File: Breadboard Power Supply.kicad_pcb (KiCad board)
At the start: 2 copper layers, 53.6 x 23.2 mm, 27 parts, among them J1 USB-C, J10 Conn_01x02_Male, J11 Conn_01x02_Male, J2 Conn_02x03_Odd_Even, J3 Conn_02x03_Odd_Even, J8 Conn_01x02_Male, J9 Conn_01x02_Male, U1 LM1117-1.8, U2 LM1117-3.3

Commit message: Updated the version number.
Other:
- board text added: "7"
- board text removed: "6"
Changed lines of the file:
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@@
     (title "Breadboard Power Supply")
     (date "2023-04-30")
-    (rev "v6")
+    (rev "v7")
   )
   (layers
@@
   (gr_line (start 155.067 98.425) (end 155.067 75.184)
     (stroke (width 0.1) (type solid)) (layer "Edge.Cuts"))
-  (gr_text "6" (at 133.477 75.946) (layer "F.Cu")
+  (gr_text "7" (at 133.477 75.946) (layer "F.Cu")
     (effects (font (size 0.5 0.5) (thickness 0.08)))
   )

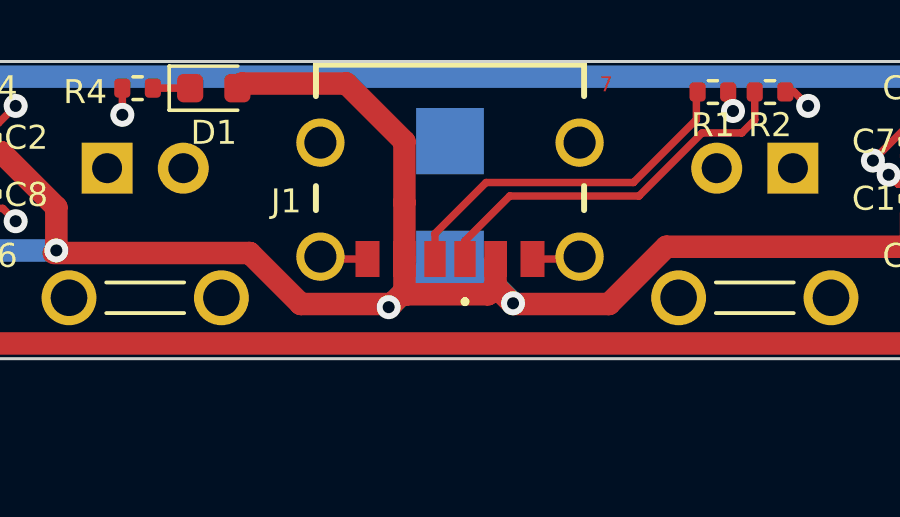
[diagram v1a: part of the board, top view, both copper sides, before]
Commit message: Replaced the Zener diode's footprint with one in the default library.
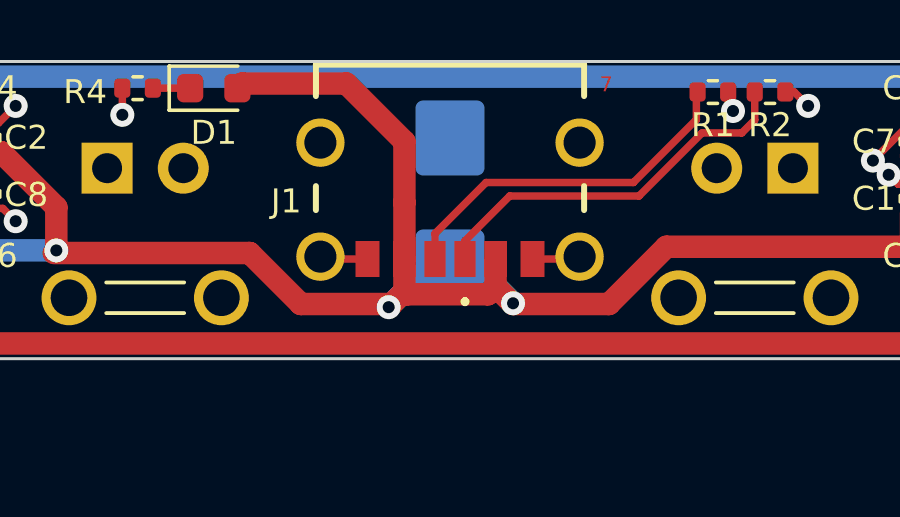
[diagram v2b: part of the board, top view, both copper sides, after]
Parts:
- D2: footprint My-Global-Footprints:SMB_STM -> Diode_SMD:D_SMB

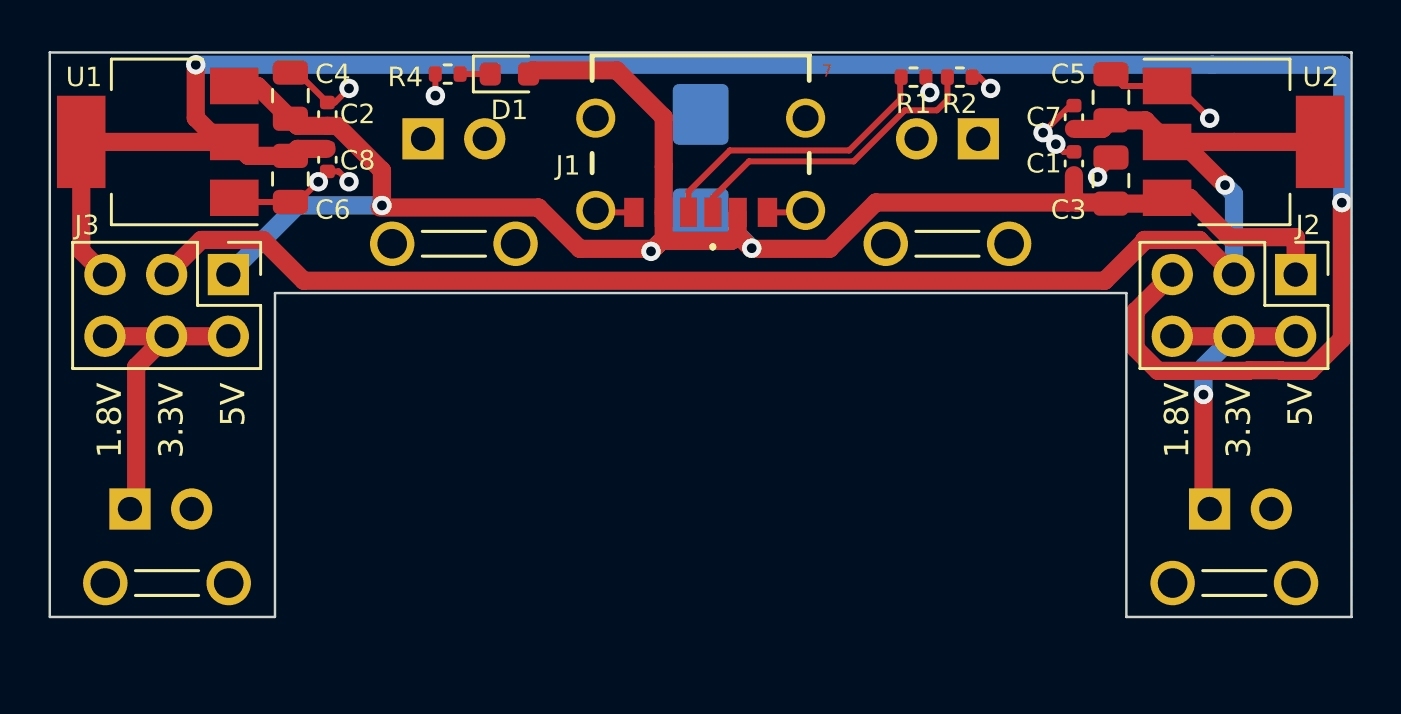
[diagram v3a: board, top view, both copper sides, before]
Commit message: Placed LEDs near voltage regulators.
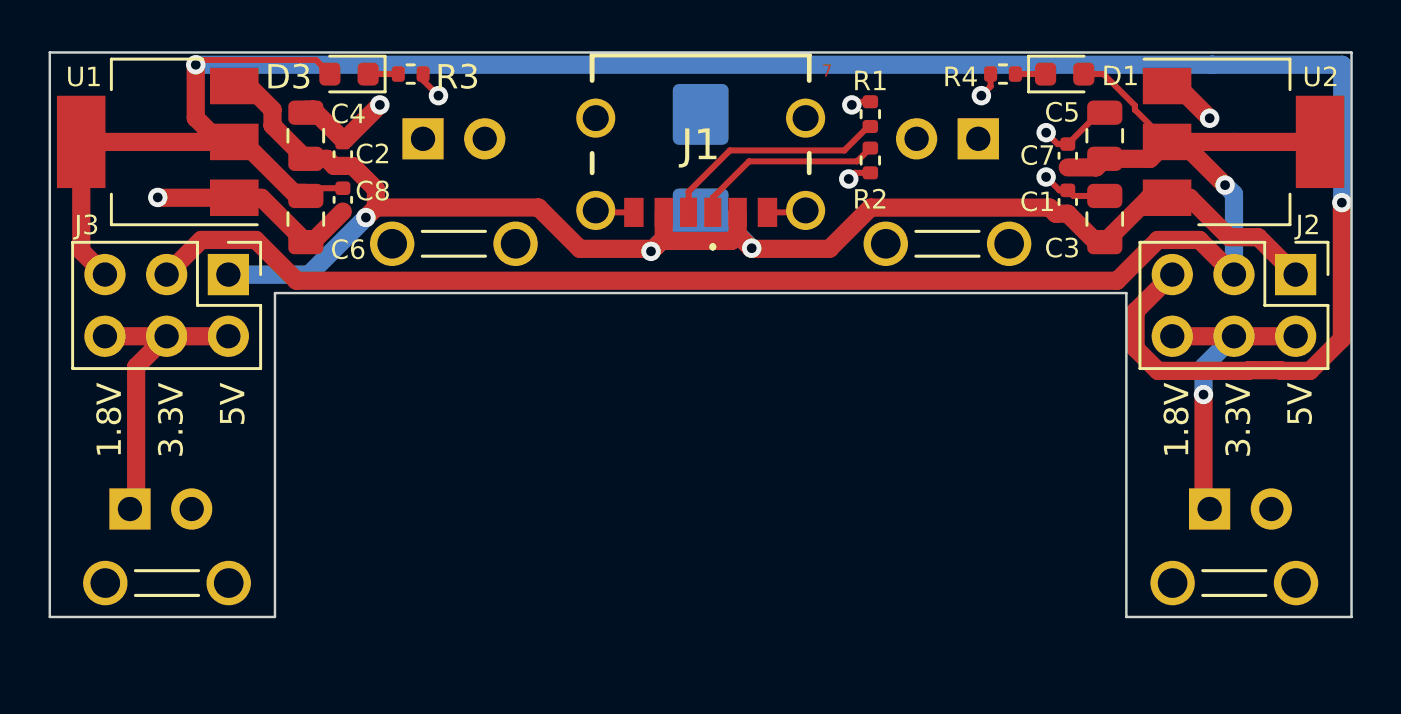
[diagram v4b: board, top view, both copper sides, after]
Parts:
- added D3: LED, LED_SMD:LED_0603_1608Metric, F.Cu at (113.8, 76.1)
- added R3: 1k, Resistor_SMD:R_0402_1005Metric, F.Cu at (116.3, 76.1)
- moved R4 22.9 mm to (140.7, 76.1)
- moved D1 22.9 mm to (143.3, 76.1)
- moved R2 5.03 mm to (135.3, 79.6), turned to -90 degrees
- moved R1 2.34 mm to (135.3, 77.7), turned to 90 degrees
- moved C2 1.77 mm to (113.5, 79.4)
- moved C4 1.77 mm to (112.0, 78.6)
- moved C6 1.77 mm to (112.0, 82.0)
- moved C8 1.77 mm to (113.5, 81.3)
- moved C3 1.61 mm to (144.9, 82.0)
- moved C7 1.61 mm to (143.4, 79.4)
- moved C1 1.61 mm to (143.4, 81.3)
- moved C5 1.61 mm to (144.9, 78.6)
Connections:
- D1 pad 2: +5V -> +3.3V
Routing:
- net +5V: track 77.5 -> 65.9 mm
- net +1V8: track 92.1 -> 99.6 mm
- net GND: track 22.3 -> 28.4 mm, vias 10 -> 9
- net Net-(J1-CC1): track 12.9 -> 7.94 mm
- net +3.3V: track 64.2 -> 69.0 mm
- net Net-(J1-CC2): track 12.1 -> 9.45 mm
- net Net-(D3-K): track 0.00 -> 1.24 mm

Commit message: Added a symbol for the OSHW logo.
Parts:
- removed REF**: OSHW-Logo_5.7x6mm_SilkScreen, Symbol:OSHW-Logo_5.7x6mm_SilkScreen
- added SYM1: Logo_Open_Hardware_Small, Symbol:OSHW-Logo_5.7x6mm_SilkScreen, B.Cu at (108.7, 78.5)

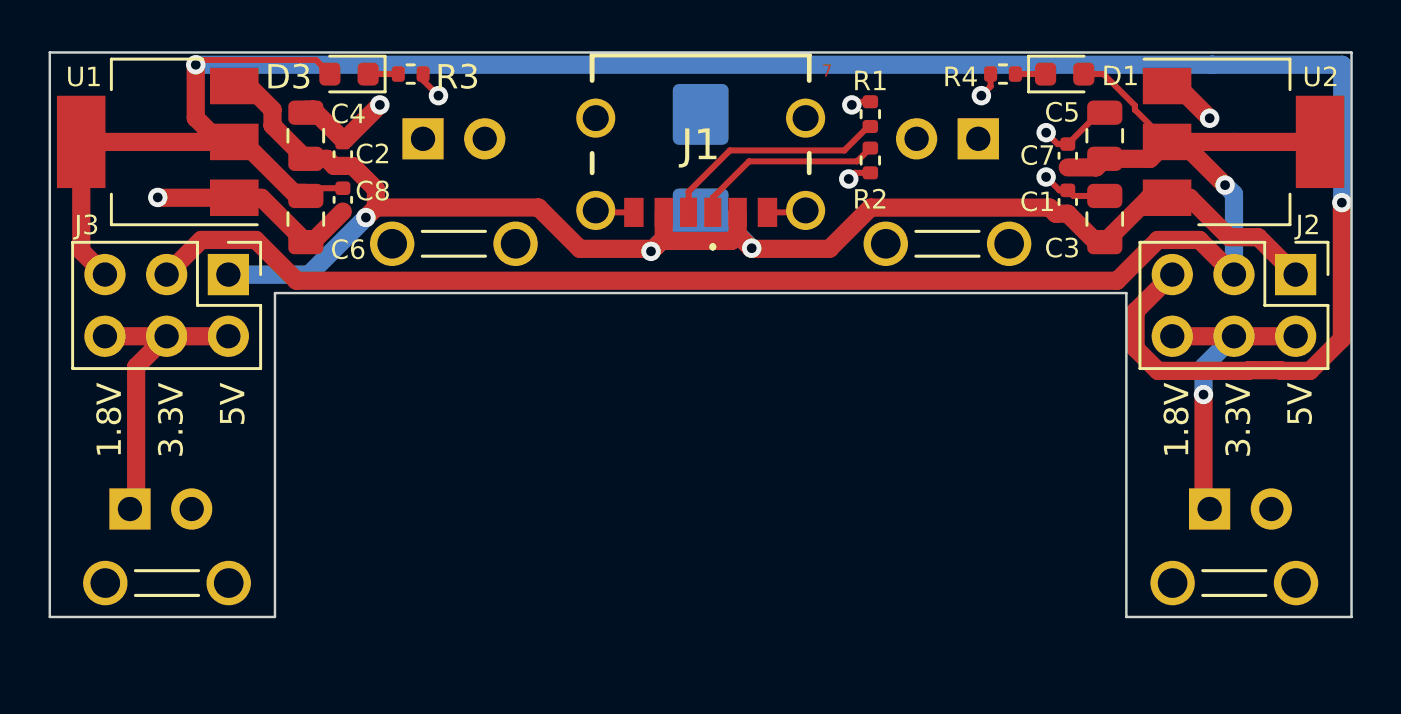
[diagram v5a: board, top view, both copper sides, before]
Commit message: Moved the USB-C to the local footprints library.
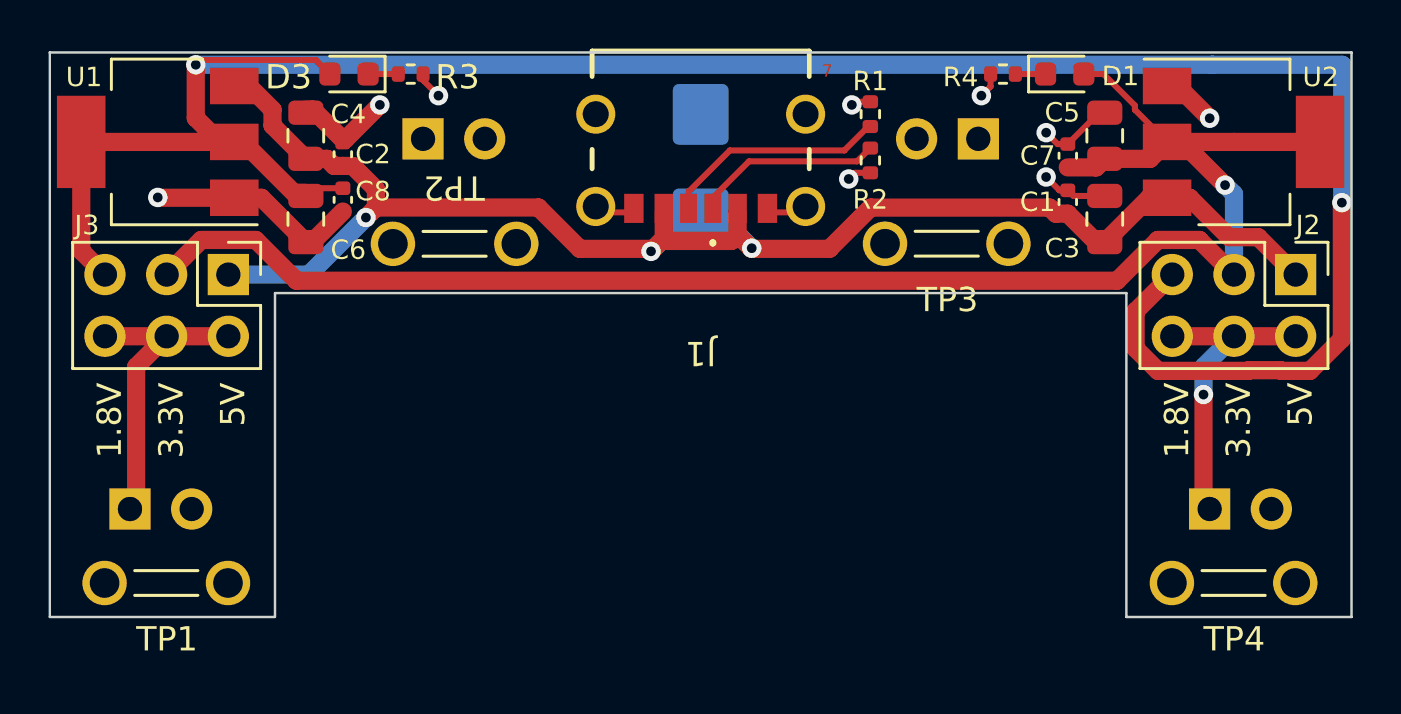
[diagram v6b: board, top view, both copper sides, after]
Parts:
- J1: footprint My-Global-Footprints:USB-C Surface Mount -> My-Local-Footprints:USB-C Power Only
- TP1, TP2, TP3, TP4: footprint My-Global-Footprints:Keystone 1430-1 -> My-Local-Footprints:Keystone 1430-1
- moved J1 0.09 mm to (128.3, 78.8)

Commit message: Added some copper fills to the PCB.
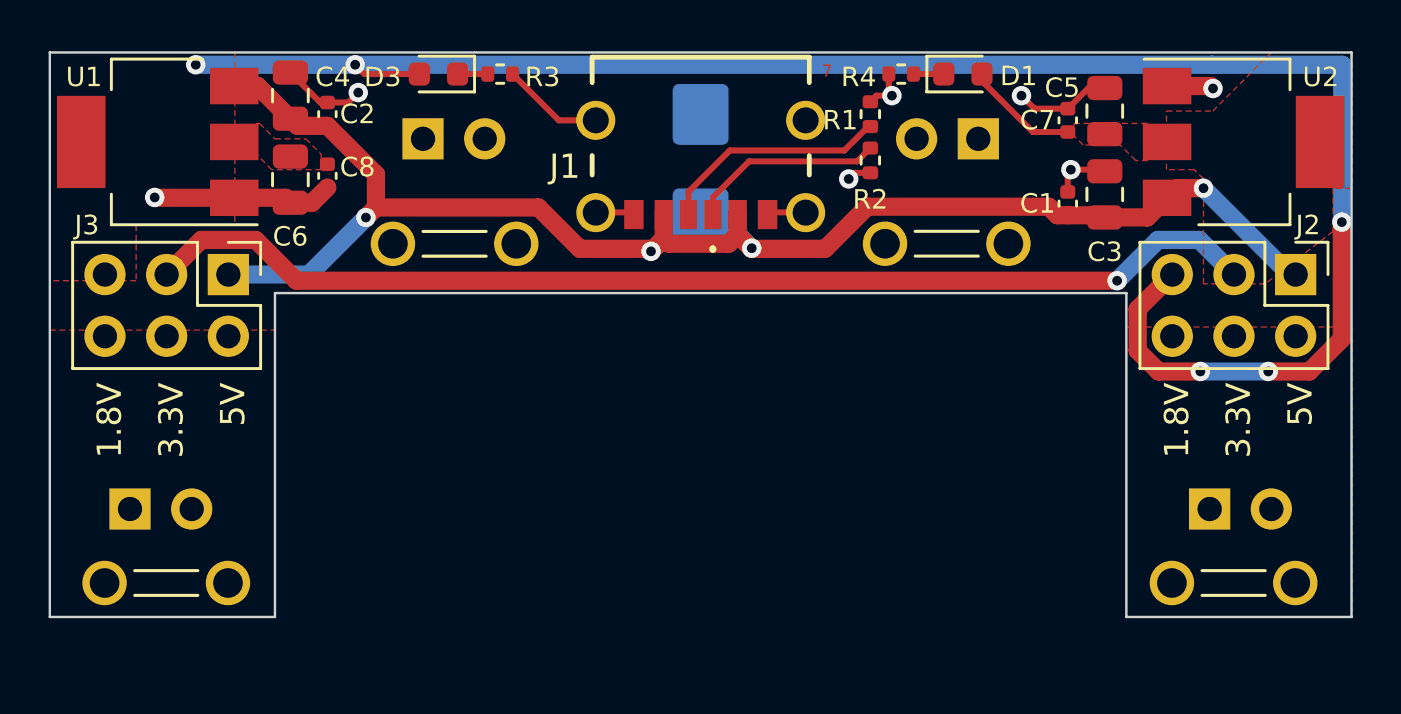
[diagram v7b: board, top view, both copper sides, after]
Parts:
- moved D1 4.19 mm to (139.1, 76.1)
- moved R4 4.19 mm to (136.5, 76.1)
- moved R3 3.68 mm to (120.0, 76.1)
- moved D3 3.68 mm to (117.5, 76.1)
- moved C2 1.77 mm to (112.9, 77.7)
- moved C4 1.77 mm to (111.4, 77.0)
- moved C6 1.74 mm to (111.4, 80.4)
- moved C7 1.46 mm to (143.4, 78.0)
- moved C8 1.17 mm to (112.9, 80.3)
- moved C3 1.02 mm to (144.9, 81.0)
- moved C5 1.02 mm to (144.9, 77.6)
- moved J1 0.25 mm to (128.3, 79.1)
- moved C1 0.07 mm to (143.4, 81.4)
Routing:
- net +1V8: track 99.6 -> 74.3 mm, vias 2 -> 5
- net +3.3V: track 69.0 -> 51.8 mm
- net /BOTTOM_POWER_RAIL: track 12.8 -> 0.00 mm
- net /TOP_POWER_RAIL: track 12.8 -> 0.00 mm, vias 1 -> 0
- net GND: track 28.4 -> 29.2 mm, vias 9 -> 7
- net +5V: track 65.9 -> 65.5 mm, vias 3 -> 4
- added copper zone on F.Cu, net +1V8
- added copper zone on F.Cu, net +3.3V
- added copper zone on F.Cu, net /BOTTOM_POWER_RAIL
- added copper zone on F.Cu, net /TOP_POWER_RAIL

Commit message: Updated BOM.
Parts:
- R3, R4: value 1k -> 470
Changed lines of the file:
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@@
         (effects (font (size 0.8 0.8) (thickness 0.1)) (justify left))
     )
-    (fp_text value "1k" (at 0 1.17) (layer "F.Fab")
+    (fp_text value "470" (at 0 1.17) (layer "F.Fab")
         (effects (font (size 1 1) (thickness 0.15)))
     )
@@
         (effects (font (size 0.8 0.8) (thickness 0.1)) (justify right))
     )
-    (fp_text value "1k" (at 0 1.17) (layer "F.Fab")
-        (effects (font (size 1 1) (thickness 0.15)))
-    )
+    (fp_text value "470" (at 0 1.17) (layer "F.Fab")
+        (effects (font (size 1 1) (thickness 0.15)))
+    )
